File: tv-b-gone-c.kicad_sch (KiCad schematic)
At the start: 26 parts, among them J2 USB4515, Q1 MMBT3904, Q2 MMBT3904, Q3 MMBT3904, Q4 MMBT3904, Q5 MMBT2907A, U1 ATtiny85V-10S, Y1 8MHz

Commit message: Update values post-fab, fix trace
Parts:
- C1: value C -> 100n
- R1: value 10k -> 100
- R3: value R -> ~680
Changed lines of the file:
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@@
 			)
 		)
-		(property "Value" "C"
+		(property "Value" "100n"
 			(at 92.71 30.4799 0)
 			(effects
@@
 			)
 		)
-		(property "Value" "R"
+		(property "Value" "~680"
 			(at 142.24 86.3599 0)
 			(effects
@@
 			)
 		)
-		(property "Value" "10k"
+		(property "Value" "100"
 			(at 184.15 50.8 90)
 			(effects

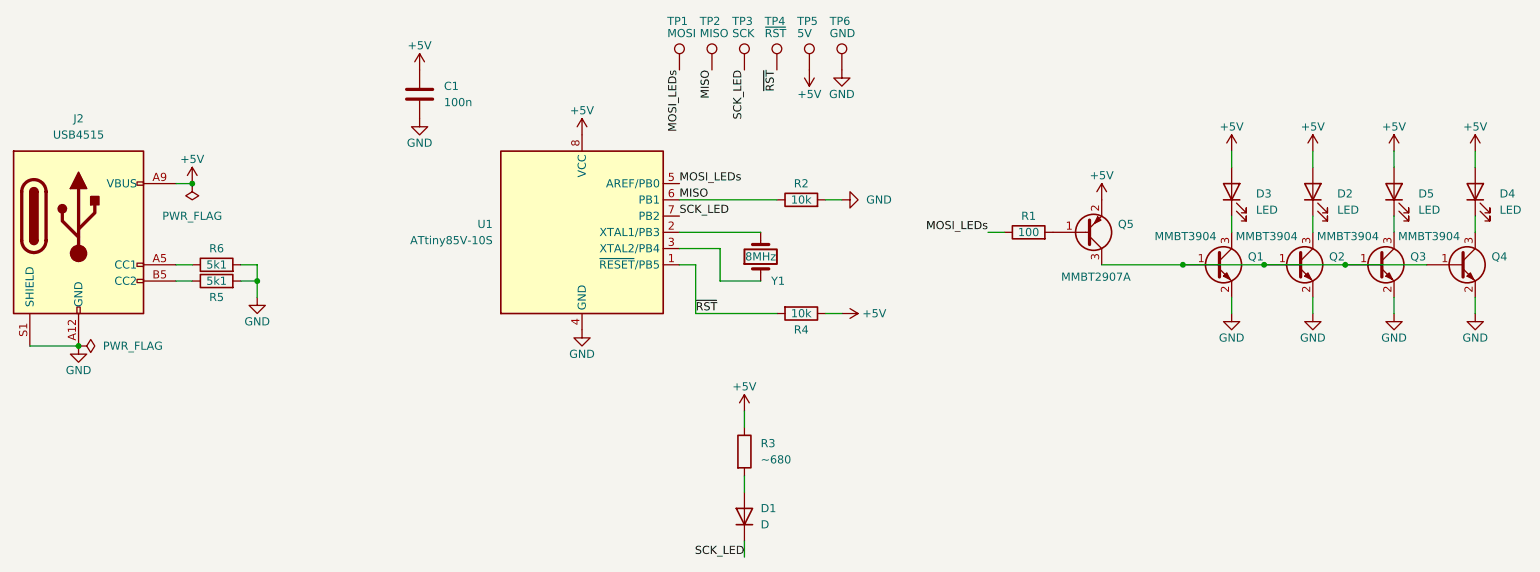
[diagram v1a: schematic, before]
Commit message: Add reset button, use mosfet
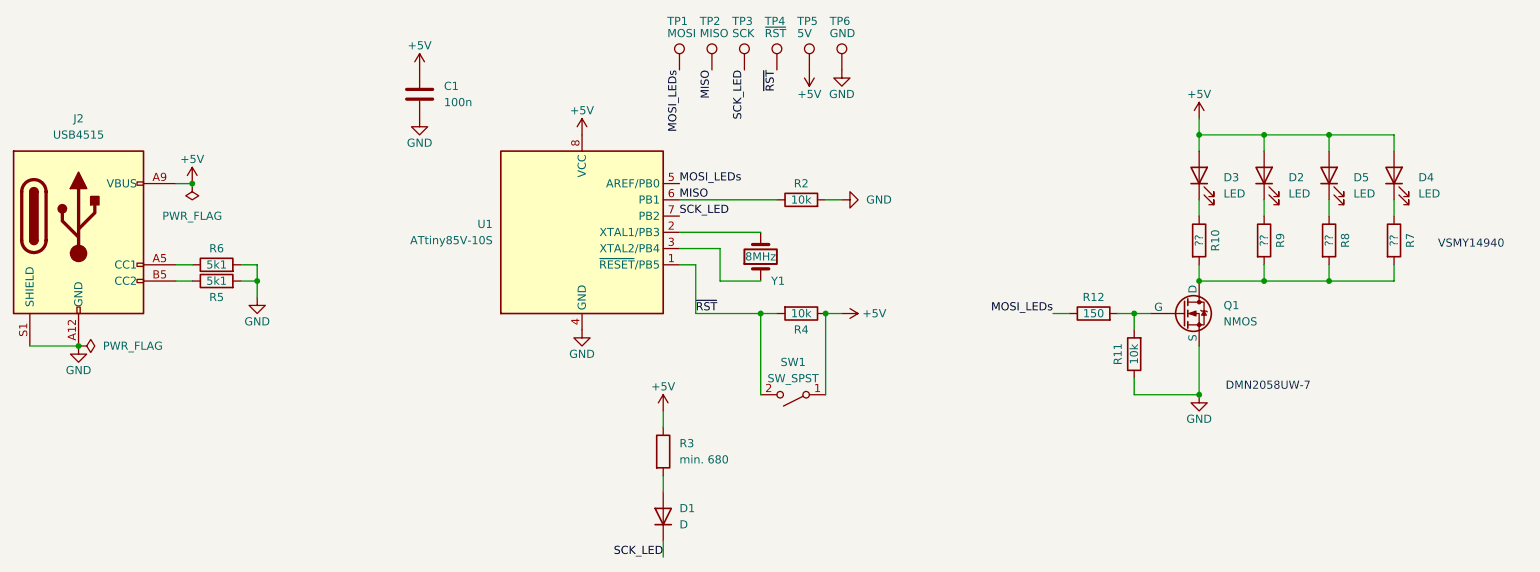
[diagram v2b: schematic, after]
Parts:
- removed Q1, Q2, Q3, Q4: MMBT3904, Package_TO_SOT_SMD:SOT-23, symbol Transistor_BJT:MMBT3904
- removed Q5: MMBT2907A, Package_TO_SOT_SMD:SOT-23, symbol Transistor_BJT:MMBTA94
- removed R1: 100, Resistor_SMD:R_0805_2012Metric_Pad1.20x1.40mm_HandSolder, symbol Device:R
- added Q1: NMOS, symbol Simulation_SPICE:NMOS
- added R10, R7, R8, R9: ??, Resistor_SMD:R_0805_2012Metric_Pad1.20x1.40mm_HandSolder, symbol Device:R
- added R11: 10k, Resistor_SMD:R_0805_2012Metric_Pad1.20x1.40mm_HandSolder, symbol Device:R
- added R12: 150, Resistor_SMD:R_0805_2012Metric_Pad1.20x1.40mm_HandSolder, symbol Device:R
- added SW1: SW_SPST, Button_Switch_SMD:SW_SPST_B3U-1000P, symbol Switch:SW_SPST
- R3: value ~680 -> min. 680
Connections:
- net +5V: now also SW1.1 (A)
- net GND: now also Q1.3 (S), R11.1
- net MOSI_LEDs: now also R12.1
- net ~{RST}: now also SW1.2 (B)
- net at D2.1 (K): now also R9.1
- net at D4.1 (K): now also R7.1
- net at D3.1 (K): now also R10.1
- net at D5.1 (K): now also R8.1
- new net: Q1.1 (D), R10.2, R7.2, R8.2, R9.2
- new net: Q1.2 (G), R11.2, R12.2
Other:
- note added: "DMN2058UW-7"
- note added: "VSMY14940"
- moved on the sheet: D1, D2, D3, D4, D5, R3
